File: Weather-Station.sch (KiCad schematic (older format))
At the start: 57 parts

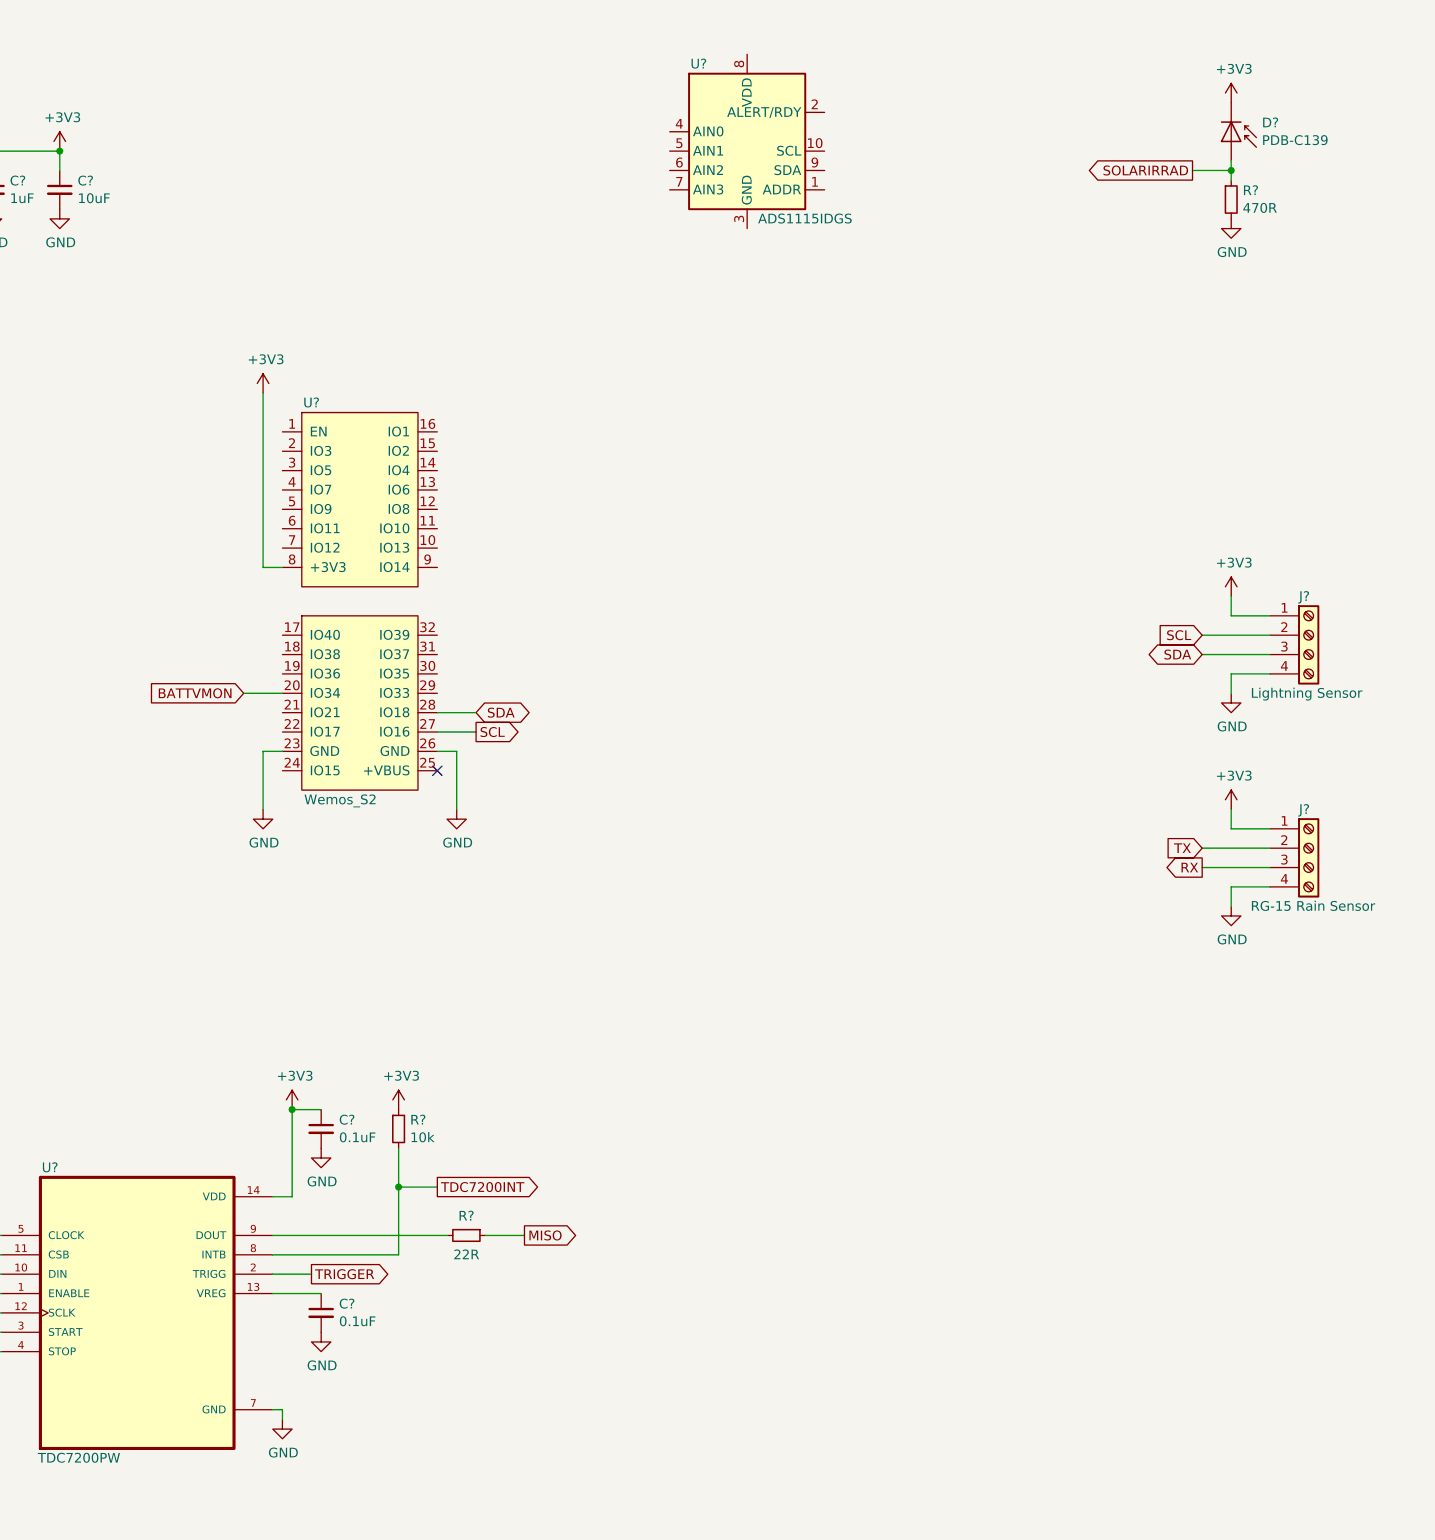
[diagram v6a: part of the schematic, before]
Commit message: added sensor interfaces
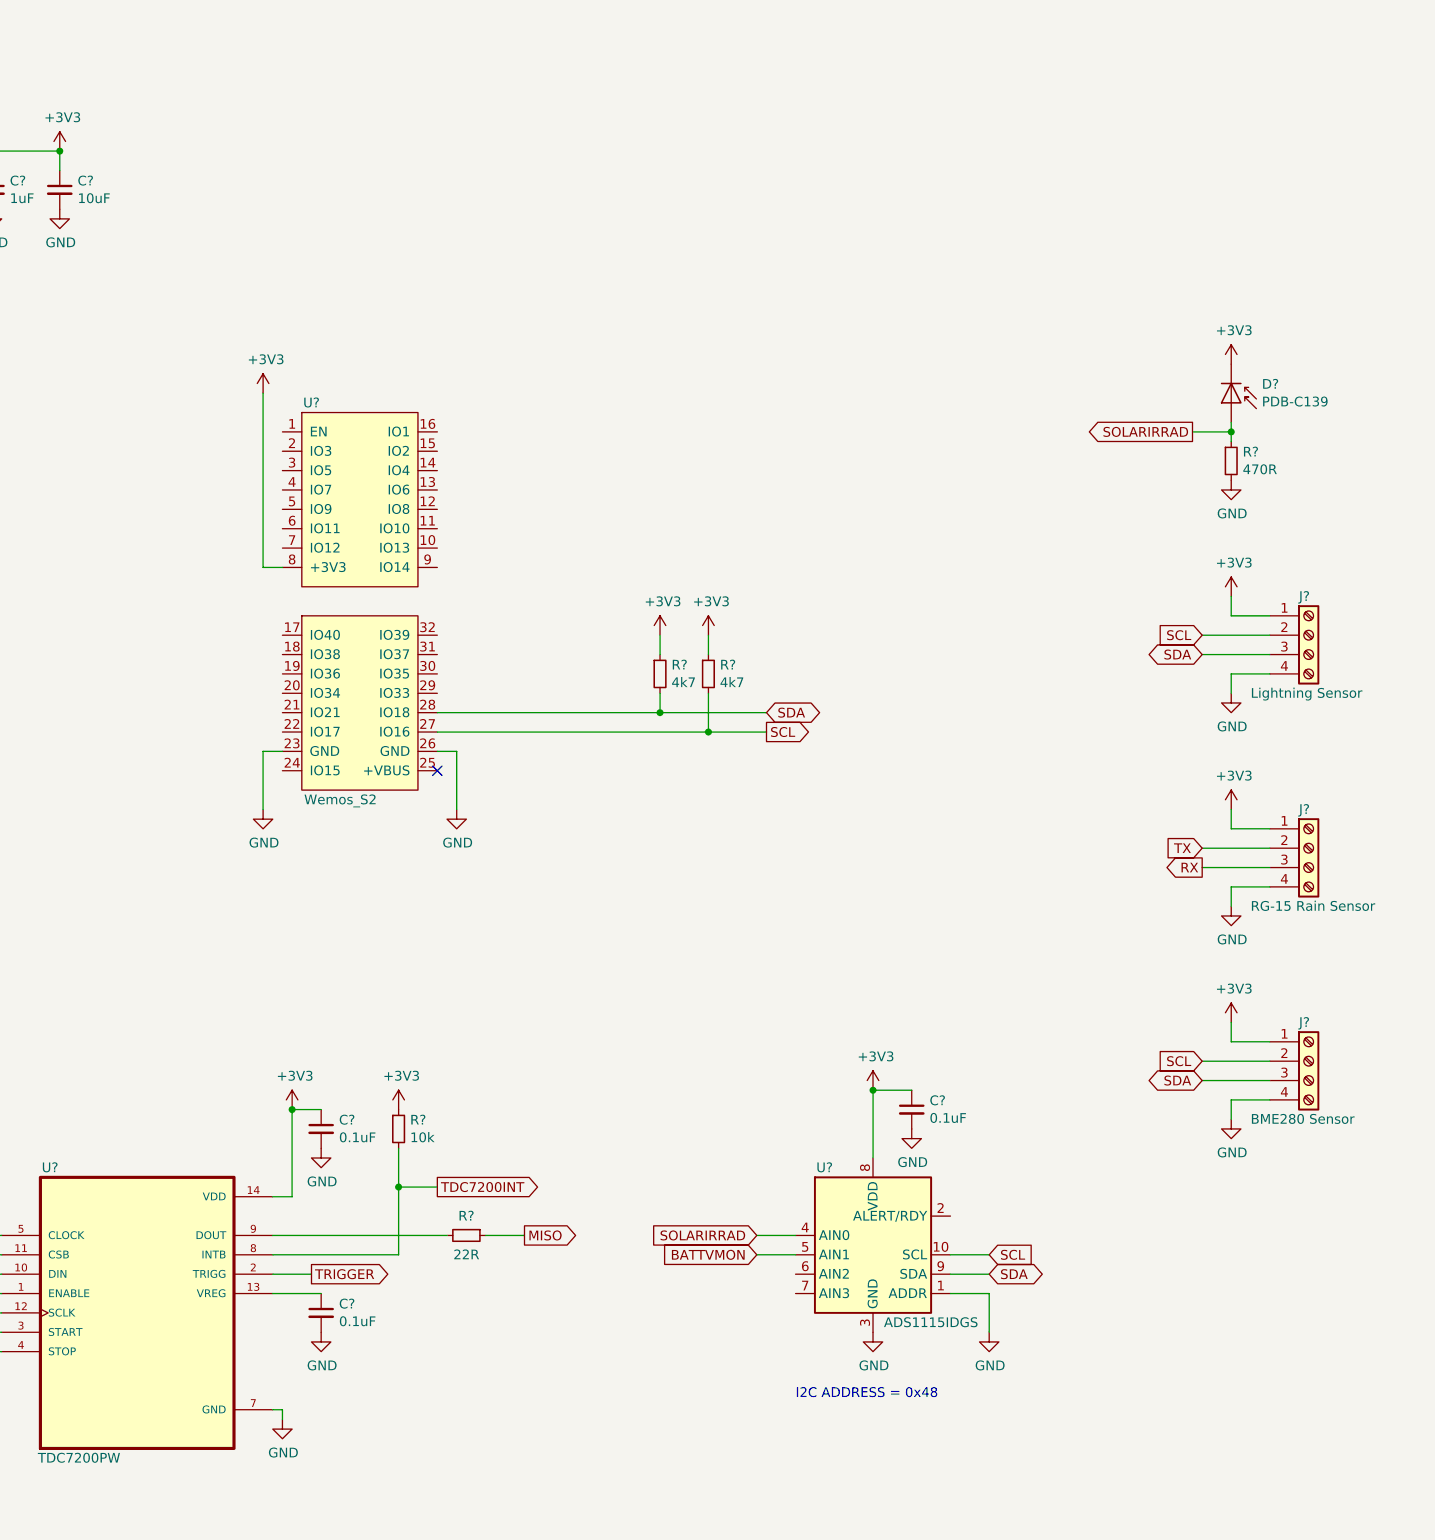
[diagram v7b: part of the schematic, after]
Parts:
- added C?: 0.1uF, Capacitor_SMD:C_0805_2012Metric, symbol Device:C_Small
- added J?: BME280 Sensor, TerminalBlock:TerminalBlock_bornier-4_P5.08mm, symbol Connector:Screw_Terminal_01x04
- added R? (x2): 4k7, Resistor_SMD:R_0805_2012Metric, symbol Device:R_Small
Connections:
- net +3V3: now also U?.8 (VDD), C?.1, J?.1 (Pin_1), R?.1, R?.1
- net BATTVMON: now also U?.5 (AIN1); no longer U?.20 (IO34)
- net GND: now also U?.1 (ADDR), U?.3 (GND), C?.2, J?.4 (Pin_4)
- net SCL: now also U?.10 (SCL), J?.2 (Pin_2), R?.2
- net SDA: now also U?.9 (SDA), J?.3 (Pin_3), R?.2
- net SOLARIRRAD: now also U?.4 (AIN0)
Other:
- note added: "I2C ADDRESS = 0x48"
- moved on the sheet: D?, R?, U?

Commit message: Finished schematic
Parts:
- added RT?: TMP36GT9Z, TO-92, symbol TMP36GT9Z:TMP36GT9Z
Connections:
- net +3V3: now also RT?.1 (VS+); no longer D?.1 (K)
- net ERRB: now also U?.11 (IO10)
- net GND: now also RT?.3 (GND); no longer R?.2
- net MISO: now also U?.19 (IO36)
- net MOSI: now also U?.31 (IO37)
- net RX: now also U?.4 (IO7)
- net SCK: now also U?.30 (IO35)
- net TDC1000CSB: now also U?.20 (IO34)
- net TDC1000EN: now also U?.6 (IO11)
- net TDC1000RESET: now also U?.10 (IO13)
- net TDC7200CSB: now also U?.29 (IO33)
- net TDC7200EN: now also U?.7 (IO12)
- net TDC7200INT: now also U?.9 (IO14)
- net TX: now also U?.5 (IO9)
- net A2: now reaches U?.6 (AIN2)
- net A2: now also RT?.2 (VOUT)
- net A3: now reaches U?.7 (AIN3)
- net A3: now also R?.1, R?.2
- removed net BATTVMON: R?.1, R?.2, U?.5 (AIN1)
- net SOLARIRRAD renamed A0
- net A0: now also D?.1 (K); no longer D?.2 (A)
- new net A1: D?.2 (A), R?.2, U?.5 (AIN1)
- no-connect marks 1 -> 15
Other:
- moved on the sheet: D?, R?
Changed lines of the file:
@@
 Text Notes 4500 3350 0    50   ~ 0
 Vhigh = 4.4V approx.\nVlow = 3.375V approx.
-Text GLabel 11750 7550 0    50   Input ~ 0
-BATTVMON
-Text GLabel 6000 2950 2    50   Output ~ 0
-BATTVMON
+Text GLabel 11750 7750 0    50   Input ~ 0
+A3
 $Comp
 L Device:R_Small R?
@@
 L Device:D_Photo D?
 U 1 1 619F7CEC
-P 14200 3150
-F 0 "D?" V 14104 3308 50  0000 L CNN
-F 1 "PDB-C139" V 14195 3308 50  0000 L CNN
-F 2 "" H 14150 3150 50  0001 C CNN
-F 3 "~" H 14150 3150 50  0001 C CNN
-	1    14200 3150
+P 14200 2550
+F 0 "D?" V 14104 2708 50  0000 L CNN
+F 1 "PDB-C139" V 14195 2708 50  0000 L CNN
+F 2 "" H 14150 2550 50  0001 C CNN
+F 3 "~" H 14150 2550 50  0001 C CNN
+	1    14200 2550
 	0    1    1    0
 $EndComp
@@
 L Device:R_Small R?
 U 1 1 619F8699
-P 14200 3450
-F 0 "R?" H 14259 3496 50  0000 L CNN
-F 1 "470R" H 14259 3405 50  0000 L CNN
-F 2 "Resistor_SMD:R_0805_2012Metric" H 14200 3450 50  0001 C CNN
-F 3 "~" H 14200 3450 50  0001 C CNN
-	1    14200 3450
-	1    0    0    -1
-$EndComp
-$Comp
-L power:GND #PWR?
-U 1 1 619F9126
-P 14200 3550
-F 0 "#PWR?" H 14200 3300 50  0001 C CNN
-F 1 "GND" H 14205 3377 50  0000 C CNN
-F 2 "" H 14200 3550 50  0001 C CNN
-F 3 "" H 14200 3550 50  0001 C CNN
-	1    14200 3550
-	1    0    0    -1
-$EndComp
-$Comp
-L power:+3V3 #PWR?
-U 1 1 619F9743
-P 14200 2950
-F 0 "#PWR?" H 14200 2800 50  0001 C CNN
-F 1 "+3V3" H 14215 3123 50  0000 C CNN
-F 2 "" H 14200 2950 50  0001 C CNN
-F 3 "" H 14200 2950 50  0001 C CNN
-	1    14200 2950
-	1    0    0    -1
-$EndComp
-Text GLabel 14000 3300 0    50   Output ~ 0
-SOLARIRRAD
-Wire Wire Line
-	14200 3350 14200 3300
-Wire Wire Line
-	14000 3300 14200 3300
-Connection ~ 14200 3300
-Wire Wire Line
-	14200 3300 14200 3250
+P 13900 2500
+F 0 "R?" H 13959 2546 50  0000 L CNN
+F 1 "470R" H 13959 2455 50  0000 L CNN
+F 2 "Resistor_SMD:R_0805_2012Metric" H 13900 2500 50  0001 C CNN
+F 3 "~" H 13900 2500 50  0001 C CNN
+	1    13900 2500
+	1    0    0    -1
+$EndComp
 $Comp
 L Analog_ADC:ADS1115IDGS U?
@@
 	12350 7050 12350 6700
 Connection ~ 12350 6700
-Text GLabel 11750 7450 0    50   Input ~ 0
-SOLARIRRAD
 Wire Wire Line
 	11750 7450 11950 7450
-Wire Wire Line
-	11750 7550 11950 7550
 Text GLabel 14050 6650 0    50   BiDi ~ 0
 SDA
@@
 Wire Wire Line
 	14200 6750 14200 6850
+Wire Wire Line
+	11750 7750 11950 7750
+Text GLabel 11750 7450 0    50   Input ~ 0
+A0
+Text GLabel 11750 7550 0    50   Input ~ 0
+A1
+Wire Wire Line
+	11950 7550 11750 7550
+Text GLabel 13700 2350 0    50   Output ~ 0
+A0
+Text GLabel 13700 2650 0    50   Output ~ 0
+A1
+Wire Wire Line
+	14200 2650 13900 2650
+Wire Wire Line
+	13900 2650 13900 2600
+Wire Wire Line
+	14200 2350 13900 2350
+Wire Wire Line
+	13900 2350 13900 2400
+Wire Wire Line
+	13700 2350 13900 2350
+Connection ~ 13900 2350
+Wire Wire Line
+	13700 2650 13900 2650
+Connection ~ 13900 2650
+$Comp
+L TMP36GT9Z:TMP36GT9Z RT?
+U 1 1 61B2AD8B
+P 14000 3200
+F 0 "RT?" H 14728 3146 50  0000 L CNN
+F 1 "TMP36GT9Z" H 14728 3055 50  0000 L CNN
+F 2 "TO-92" H 14750 3300 50  0001 L CNN
+F 3 "https://datasheet.datasheetarchive.com/originals/distributors/SFDatasheet-4/sf-00085637.pdf" H 14750 3200 50  0001 L CNN
+F 4 "TMP36GT9Z, Temperature Sensor +/-3C Serial-2 Wire 2.7  5.5 V 3-Pin TO-92" H 14750 3100 50  0001 L CNN "Description"
+F 5 "" H 14750 3000 50  0001 L CNN "Height"
+F 6 "Analog Devices" H 14750 2900 50  0001 L CNN "Manufacturer_Name"
+F 7 "TMP36GT9Z" H 14750 2800 50  0001 L CNN "Manufacturer_Part_Number"
+F 8 "584-TMP36GT9Z" H 14750 2700 50  0001 L CNN "Mouser Part Number"
+F 9 "https://www.mouser.co.uk/ProductDetail/Analog-Devices/TMP36GT9Z?qs=WIvQP4zGanhT97N47MSoHw%3D%3D" H 14750 2600 50  0001 L CNN "Mouser Price/Stock"
+F 10 "TMP36GT9Z" H 14750 2500 50  0001 L CNN "Arrow Part Number"
+F 11 "https://www.arrow.com/en/products/tmp36gt9z/analog-devices?region=nac" H 14750 2400 50  0001 L CNN "Arrow Price/Stock"
+	1    14000 3200
+	1    0    0    -1
+$EndComp
+$Comp
+L power:GND #PWR?
+U 1 1 61B2C44F
+P 13900 3500
+F 0 "#PWR?" H 13900 3250 50  0001 C CNN
+F 1 "GND" H 13905 3327 50  0000 C CNN
+F 2 "" H 13900 3500 50  0001 C CNN
+F 3 "" H 13900 3500 50  0001 C CNN
+	1    13900 3500
+	1    0    0    -1
+$EndComp
+Wire Wire Line
+	13900 3500 13900 3200
+Wire Wire Line
+	13900 3200 14000 3200
+Text GLabel 11750 7650 0    50   Input ~ 0
+A2
+Text GLabel 13700 3300 0    50   Output ~ 0
+A2
+Wire Wire Line
+	13700 3300 14000 3300
+$Comp
+L power:+3V3 #PWR?
+U 1 1 61B45FB8
+P 13800 3100
+F 0 "#PWR?" H 13800 2950 50  0001 C CNN
+F 1 "+3V3" H 13815 3273 50  0000 C CNN
+F 2 "" H 13800 3100 50  0001 C CNN
+F 3 "" H 13800 3100 50  0001 C CNN
+	1    13800 3100
+	1    0    0    -1
+$EndComp
+Wire Wire Line
+	14000 3400 13800 3400
+Wire Wire Line
+	13800 3400 13800 3100
+Wire Wire Line
+	11950 7650 11750 7650
+Text GLabel 6000 2950 2    50   Output ~ 0
+A3
+Wire Wire Line
+	9300 3600 8950 3600
+Wire Wire Line
+	8950 3700 9300 3700
+Text GLabel 8950 3700 0    50   Output ~ 0
+TX
+Text GLabel 8950 3600 0    50   Input ~ 0
+RX
+Text GLabel 9100 4550 0    50   Input ~ 0
+MISO
+Text GLabel 10300 4450 2    50   Output ~ 0
+MOSI
+Text GLabel 10300 4550 2    50   Output ~ 0
+SCK
+Text GLabel 9100 4650 0    50   Output ~ 0
+TDC1000CSB
+Text GLabel 10300 4650 2    50   Output ~ 0
+TDC7200CSB
+Text GLabel 8950 3800 0    50   Output ~ 0
+TDC1000EN
+Text GLabel 8950 3900 0    50   Output ~ 0
+TDC7200EN
+Text GLabel 10300 3900 2    50   Output ~ 0
+TDC1000RESET
+Text GLabel 10300 3800 2    50   Input ~ 0
+ERRB
+Text GLabel 10300 4000 2    50   Input ~ 0
+TDC7200INT
+Wire Wire Line
+	10300 4650 10100 4650
+Wire Wire Line
+	10300 4550 10100 4550
+Wire Wire Line
+	10300 4450 10100 4450
+Wire Wire Line
+	9300 4550 9100 4550
+Wire Wire Line
+	9300 4650 9100 4650
+Wire Wire Line
+	10300 3800 10100 3800
+Wire Wire Line
+	10300 3900 10100 3900
+Wire Wire Line
+	10300 4000 10100 4000
+Wire Wire Line
+	9300 3800 8950 3800
+Wire Wire Line
+	8950 3900 9300 3900
+NoConn ~ 9300 3300
+NoConn ~ 9300 3400
+NoConn ~ 9300 3500
+NoConn ~ 10100 3300
+NoConn ~ 10100 3400
+NoConn ~ 10100 3500
+NoConn ~ 10100 3600
+NoConn ~ 10100 3700
+NoConn ~ 10100 4350
+NoConn ~ 9300 4350
+NoConn ~ 9300 4450
+NoConn ~ 9300 4750
+NoConn ~ 9300 4850
+NoConn ~ 9300 5050
 $EndSCHEMATC
